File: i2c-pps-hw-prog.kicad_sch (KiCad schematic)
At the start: 0 parts

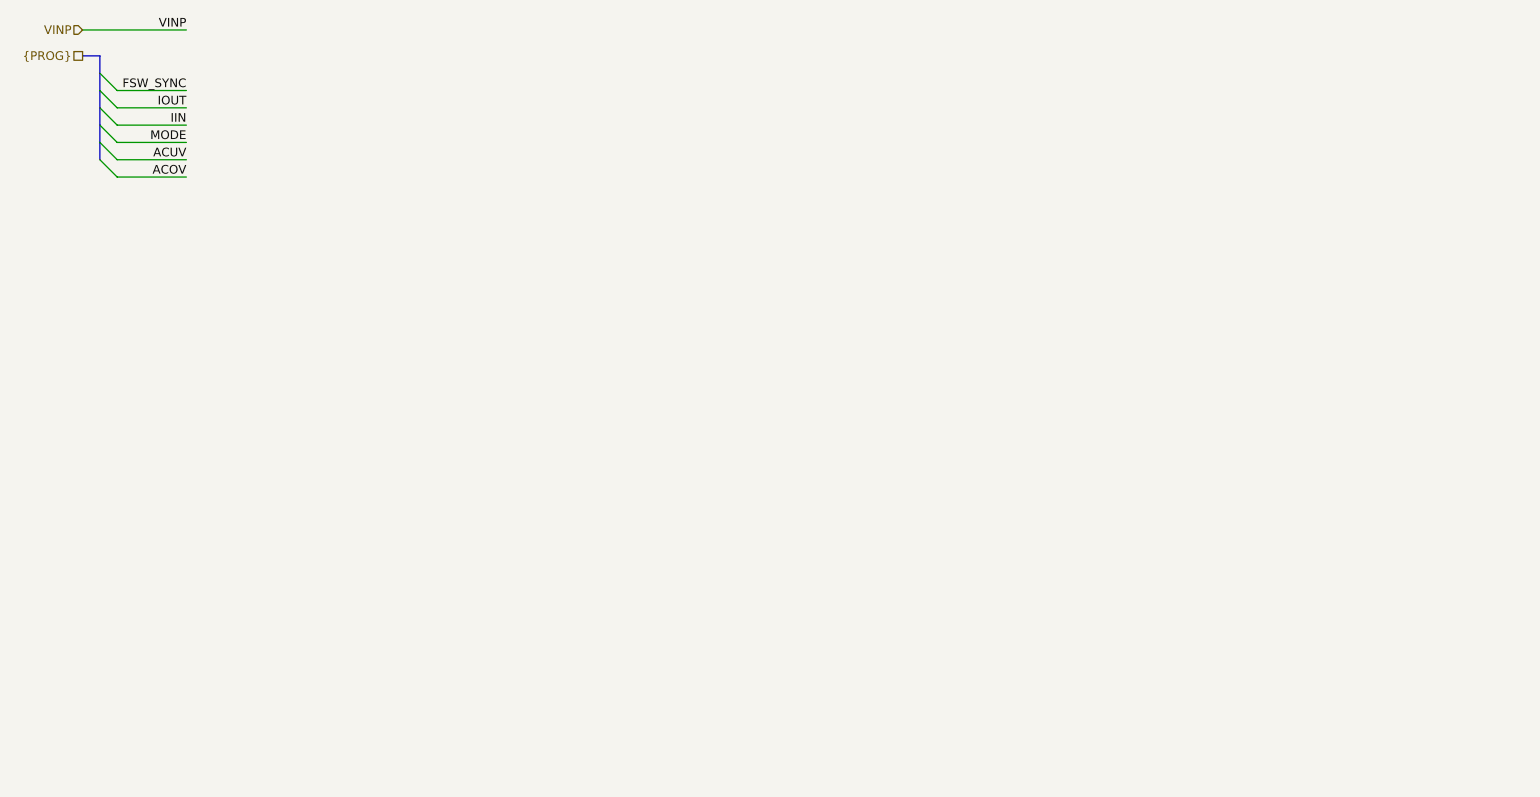
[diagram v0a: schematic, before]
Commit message: Design schematics and set per component requirements
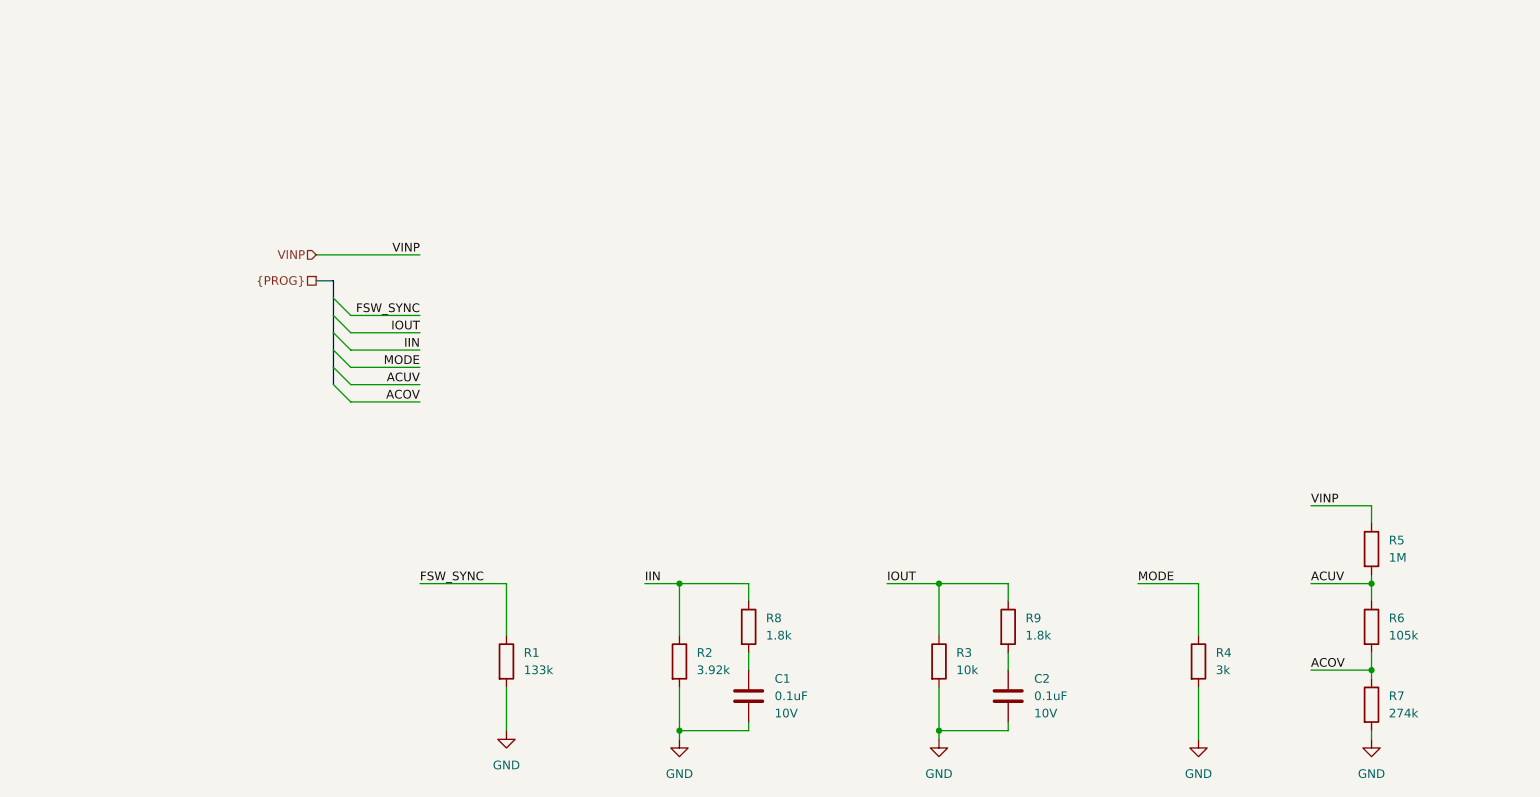
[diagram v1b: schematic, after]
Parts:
- added C1, C2: 0.1uF, Capacitor_SMD:C_0603_1608Metric_Pad1.08x0.95mm_HandSolder, symbol Device:C
- added R1: 133k, Resistor_SMD:R_0603_1608Metric_Pad0.98x0.95mm_HandSolder, symbol Device:R
- added R2: 3.92k, Resistor_SMD:R_0603_1608Metric_Pad0.98x0.95mm_HandSolder, symbol Device:R
- added R3: 10k, Resistor_SMD:R_0603_1608Metric_Pad0.98x0.95mm_HandSolder, symbol Device:R
- added R4: 3k, Resistor_SMD:R_0603_1608Metric_Pad0.98x0.95mm_HandSolder, symbol Device:R
- added R5: 1M, Resistor_SMD:R_0805_2012Metric, symbol Device:R
- added R6: 105k, Resistor_SMD:R_0805_2012Metric, symbol Device:R
- added R7: 274k, Resistor_SMD:R_0805_2012Metric, symbol Device:R
- added R8, R9: 1.8k, Resistor_SMD:R_0603_1608Metric_Pad0.98x0.95mm_HandSolder, symbol Device:R
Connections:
- net ACOV: now also R6.2, R7.1
- net ACUV: now also R5.2, R6.1
- net FSW_SYNC: now also R1.1
- net IIN: now also R2.1, R8.1
- net IOUT: now also R3.1, R9.1
- net MODE: now also R4.1
- net VINP: now also R5.1
- new net: C1.1, R8.2
- new net: C2.1, R9.2
- new net GND: C1.2, C2.2, R1.2, R2.2, R3.2, R4.2, R7.2

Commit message: Rename VINP to +5V_Run for clarity
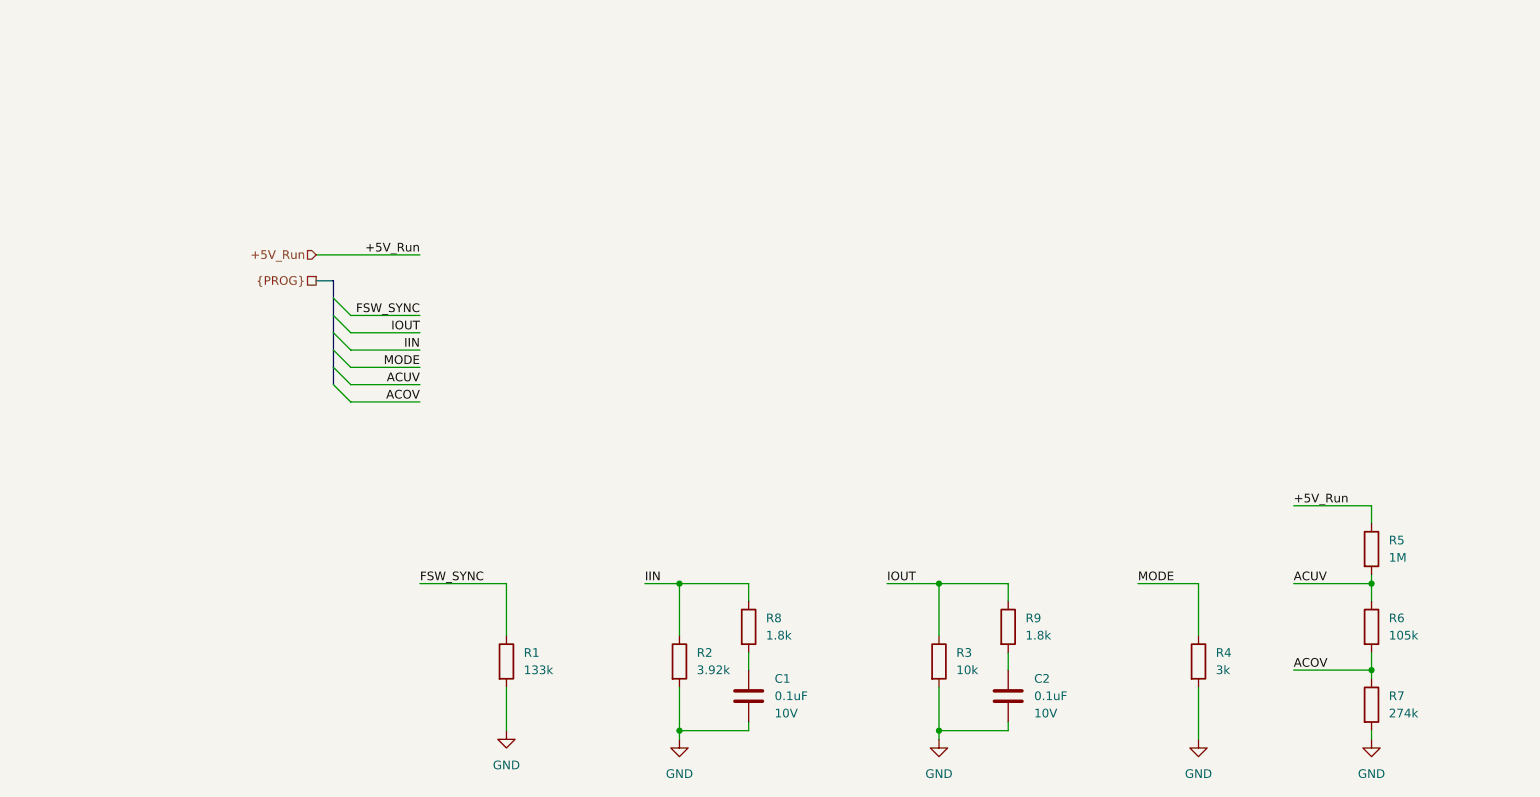
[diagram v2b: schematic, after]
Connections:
- net VINP renamed +5V_Run
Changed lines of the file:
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@@
 	(wire
 		(pts
-			(xy 205.74 95.25) (xy 214.63 95.25)
+			(xy 203.2 95.25) (xy 214.63 95.25)
 		)
 		(stroke
@@
 	(wire
 		(pts
-			(xy 205.74 119.38) (xy 214.63 119.38)
+			(xy 203.2 119.38) (xy 214.63 119.38)
 		)
 		(stroke
@@
 	(wire
 		(pts
-			(xy 205.74 106.68) (xy 214.63 106.68)
+			(xy 203.2 106.68) (xy 214.63 106.68)
 		)
 		(stroke
@@
 		)
 	)
-	(label "VINP"
-		(at 205.74 95.25 0)
+	(label "+5V_Run"
+		(at 203.2 95.25 0)
 		(effects
 			(font
@@
 	)
 	(label "ACOV"
-		(at 205.74 119.38 0)
-		(effects
-			(font
-				(size 1.27 1.27)
-			)
-			(justify left bottom)
-		)
-	)
-	(label "VINP"
+		(at 203.2 119.38 0)
+		(effects
+			(font
+				(size 1.27 1.27)
+			)
+			(justify left bottom)
+		)
+	)
+	(label "+5V_Run"
 		(at 74.93 58.42 180)
 		(effects
@@
 	)
 	(label "ACUV"
-		(at 205.74 106.68 0)
+		(at 203.2 106.68 0)
 		(effects
 			(font
@@
 		)
 	)
-	(hierarchical_label "VINP"
+	(hierarchical_label "+5V_Run"
 		(shape input)
 		(at 59.69 58.42 180)

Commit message: Select market available components
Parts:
- C1, C2: Manufacturer (none) -> KEMET; Part Number (none) -> C0603C104K8RACTU
- R1: Manufacturer (none) -> YAGEO; Part Number (none) -> RC0603FR-07133KL
- R2: Manufacturer (none) -> YAGEO; Part Number (none) -> RC0603FR-073K92L
- R3: Manufacturer (none) -> YAGEO; Part Number (none) -> RC0603FR-0710KL
- R4: Manufacturer (none) -> YAGEO; Part Number (none) -> RC0603FR-073KL
- R5: Manufacturer (none) -> Panasonic Electronic Components; Part Number (none) -> ERA-6AEB105V
- R6: Manufacturer (none) -> Panasonic Electronic Components; Part Number (none) -> ERA-6AEB1053V
- R7: Manufacturer (none) -> Panasonic Electronic Components; Part Number (none) -> ERA-6AEB2743V
- R8, R9: Manufacturer (none) -> YAGEO; Part Number (none) -> RC0603JR-071K8L
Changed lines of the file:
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@@
 			)
 		)
-		(property "Datasheet" "~"
+		(property "Datasheet" "https://yageogroup.com/content/datasheet/asset/file/PYU-RC_GROUP_51_ROHS_L"
 			(at 151.13 118.11 0)
 			(effects
@@
 			)
 		)
+		(property "Manufacturer" "YAGEO"
+			(at 151.13 118.11 0)
+			(effects
+				(font
+					(size 1.27 1.27)
+				)
+				(hide yes)
+			)
+		)
+		(property "Part Number" "RC0603FR-0710KL"
+			(at 151.13 118.11 0)
+			(effects
+				(font
+					(size 1.27 1.27)
+				)
+				(hide yes)
+			)
+		)
 		(pin "1"
 		)
@@
 			)
 		)
-		(property "Datasheet" "~"
+		(property "Datasheet" "https://yageogroup.com/content/datasheet/asset/file/KEM_C1002_X7R_SMD"
 			(at 123.19 123.19 0)
 			(effects
@@
 				)
 				(justify left)
+			)
+		)
+		(property "Manufacturer" "KEMET"
+			(at 123.19 123.19 0)
+			(effects
+				(font
+					(size 1.27 1.27)
+				)
+				(hide yes)
+			)
+		)
+		(property "Part Number" "C0603C104K8RACTU"
+			(at 123.19 123.19 0)
+			(effects
+				(font
+					(size 1.27 1.27)
+				)
+				(hide yes)
 			)
 		)
@@
 			)
 		)
-		(property "Datasheet" "~"
+		(property "Datasheet" "https://yageogroup.com/content/datasheet/asset/file/KEM_C1002_X7R_SMD"
 			(at 161.29 123.19 0)
 			(effects
@@
 				)
 				(justify left)
+			)
+		)
+		(property "Manufacturer" "KEMET"
+			(at 161.29 123.19 0)
+			(effects
+				(font
+					(size 1.27 1.27)
+				)
+				(hide yes)
+			)
+		)
+		(property "Part Number" "C0603C104K8RACTU"
+			(at 161.29 123.19 0)
+			(effects
+				(font
+					(size 1.27 1.27)
+				)
+				(hide yes)
 			)
 		)
@@
 			)
 		)
-		(property "Datasheet" "~"
+		(property "Datasheet" "https://industrial.panasonic.com/cdbs/www-data/pdf/RDM0000/AOA0000C307.pdf"
 			(at 214.63 113.03 0)
 			(effects
@@
 		)
 		(property "Description" "0.1%, 0.125W, 25ppm/°C"
+			(at 214.63 113.03 0)
+			(effects
+				(font
+					(size 1.27 1.27)
+				)
+				(hide yes)
+			)
+		)
+		(property "Manufacturer" "Panasonic Electronic Components"
+			(at 214.63 113.03 0)
+			(effects
+				(font
+					(size 1.27 1.27)
+				)
+				(hide yes)
+			)
+		)
+		(property "Part Number" "ERA-6AEB1053V"
 			(at 214.63 113.03 0)
 			(effects
@@
 			)
 		)
-		(property "Datasheet" "~"
+		(property "Datasheet" "https://yageogroup.com/content/datasheet/asset/file/PYU-RC_GROUP_51_ROHS_L"
 			(at 123.19 113.03 0)
 			(effects
@@
 		)
 		(property "Description" "5%, 0.1W"
+			(at 123.19 113.03 0)
+			(effects
+				(font
+					(size 1.27 1.27)
+				)
+				(hide yes)
+			)
+		)
+		(property "Manufacturer" "YAGEO"
+			(at 123.19 113.03 0)
+			(effects
+				(font
+					(size 1.27 1.27)
+				)
+				(hide yes)
+			)
+		)
+		(property "Part Number" "RC0603JR-071K8L"
 			(at 123.19 113.03 0)
 			(effects
@@
 			)
 		)
-		(property "Datasheet" "~"
+		(property "Datasheet" "https://industrial.panasonic.com/cdbs/www-data/pdf/RDM0000/AOA0000C307.pdf"
 			(at 214.63 101.6 0)
 			(effects
@@
 		)
 		(property "Description" "0.1%, 0.125W, 25ppm/°C"
+			(at 214.63 101.6 0)
+			(effects
+				(font
+					(size 1.27 1.27)
+				)
+				(hide yes)
+			)
+		)
+		(property "Manufacturer" "Panasonic Electronic Components"
+			(at 214.63 101.6 0)
+			(effects
+				(font
+					(size 1.27 1.27)
+				)
+				(hide yes)
+			)
+		)
+		(property "Part Number" "ERA-6AEB105V"
 			(at 214.63 101.6 0)
 			(effects
@@
 			)
 		)
-		(property "Datasheet" "~"
+		(property "Datasheet" "https://yageogroup.com/content/datasheet/asset/file/PYU-RC_GROUP_51_ROHS_L"
 			(at 161.29 113.03 0)
 			(effects
@@
 		)
 		(property "Description" "5%, 0.1W"
+			(at 161.29 113.03 0)
+			(effects
+				(font
+					(size 1.27 1.27)
+				)
+				(hide yes)
+			)
+		)
+		(property "Manufacturer" "YAGEO"
+			(at 161.29 113.03 0)
+			(effects
+				(font
+					(size 1.27 1.27)
+				)
+				(hide yes)
+			)
+		)
+		(property "Part Number" "RC0603JR-071K8L"
 			(at 161.29 113.03 0)
 			(effects
@@
 			)
 		)
-		(property "Datasheet" "~"
+		(property "Datasheet" "https://yageogroup.com/content/datasheet/asset/file/PYU-RC_GROUP_51_ROHS_L"
 			(at 87.63 118.11 0)
 			(effects
@@
 		)
 		(property "Description" "1%, 0.1W"
+			(at 87.63 118.11 0)
+			(effects
+				(font
+					(size 1.27 1.27)
+				)
+				(hide yes)
+			)
+		)
+		(property "Manufacturer" "YAGEO"
+			(at 87.63 118.11 0)
+			(effects
+				(font
+					(size 1.27 1.27)
+				)
+				(hide yes)
+			)
+		)
+		(property "Part Number" "RC0603FR-07133KL"
 			(at 87.63 118.11 0)
 			(effects
@@
 			)
 		)
-		(property "Datasheet" "~"
+		(property "Datasheet" "https://yageogroup.com/content/datasheet/asset/file/PYU-RC_GROUP_51_ROHS_L"
 			(at 189.23 118.11 0)
 			(effects
@@
 		)
 		(property "Description" "1%, 0.1W"
+			(at 189.23 118.11 0)
+			(effects
+				(font
+					(size 1.27 1.27)
+				)
+				(hide yes)
+			)
+		)
+		(property "Manufacturer" "YAGEO"
+			(at 189.23 118.11 0)
+			(effects
+				(font
+					(size 1.27 1.27)
+				)
+				(hide yes)
+			)
+		)
+		(property "Part Number" "RC0603FR-073KL"
 			(at 189.23 118.11 0)
 			(effects
@@
 			)
 		)
-		(property "Datasheet" "~"
+		(property "Datasheet" "https://yageogroup.com/content/datasheet/asset/file/PYU-RC_GROUP_51_ROHS_L"
 			(at 113.03 118.11 0)
 			(effects
@@
 		)
 		(property "Description" "1%, 0.1W"
+			(at 113.03 118.11 0)
+			(effects
+				(font
+					(size 1.27 1.27)
+				)
+				(hide yes)
+			)
+		)
+		(property "Manufacturer" "YAGEO"
+			(at 113.03 118.11 0)
+			(effects
+				(font
+					(size 1.27 1.27)
+				)
+				(hide yes)
+			)
+		)
+		(property "Part Number" "RC0603FR-073K92L"
 			(at 113.03 118.11 0)
 			(effects
@@
 			)
 		)
-		(property "Datasheet" "~"
+		(property "Datasheet" "https://industrial.panasonic.com/cdbs/www-data/pdf/RDM0000/AOA0000C307.pdf"
 			(at 214.63 124.46 0)
 			(effects
@@
 			(at 214.63 124.46 0)
 			(effects
+				(font
+					(size 1.27 1.27)
+				)
+				(hide yes)
+			)
+		)
+		(property "Manufacturer" "Panasonic Electronic Components"
+			(at 214.63 124.46 0)
+			(effects
+				(font
+					(size 1.27 1.27)
+				)
+				(hide yes)
+			)
+		)
+		(property "Part Number" "ERA-6AEB2743V"
+			(at 214.63 124.46 0)
+			(effects

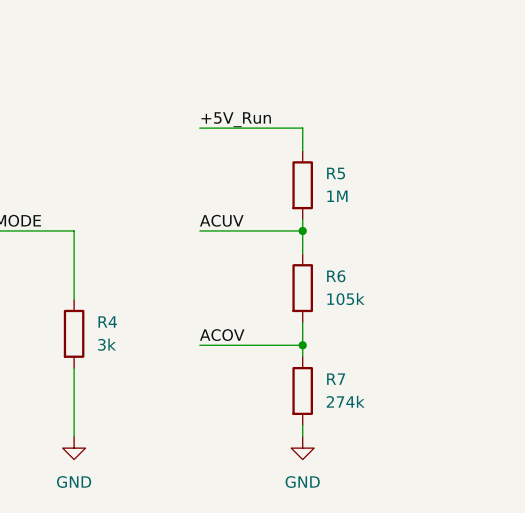
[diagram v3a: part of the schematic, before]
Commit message: Place and route controller surroundings
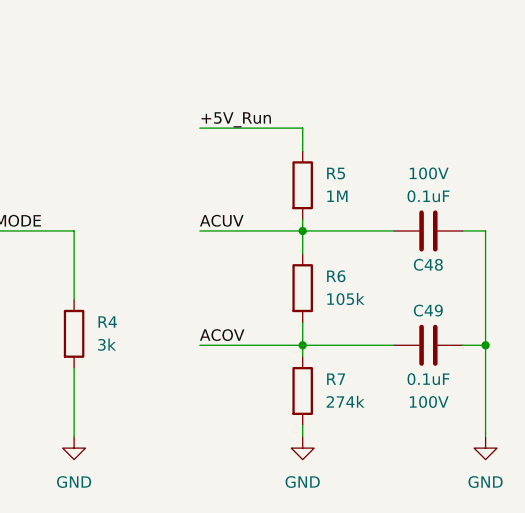
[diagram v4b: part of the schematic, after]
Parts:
- added C48, C49: 0.1uF, Capacitor_SMD:C_0603_1608Metric_Pad1.08x0.95mm_HandSolder, symbol Device:C
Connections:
- net ACOV: now also C49.1
- net ACUV: now also C48.1
- net GND: now also C48.2, C49.2
